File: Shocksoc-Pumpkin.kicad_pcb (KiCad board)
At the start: 2 copper layers, 98.7 x 98.5 mm, 45 parts, among them J1 USB_B_Micro, J2 Conn_01x03_Male, J3 Conn_01x02_Male, J4 Conn_ARM_JTAG_SWD_10, Q1 BSN20, SW1 SW_Push, SW2 SW_Push, SW3 SW_Push, SW4 SW_Push, U1 AP2202K-3.3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

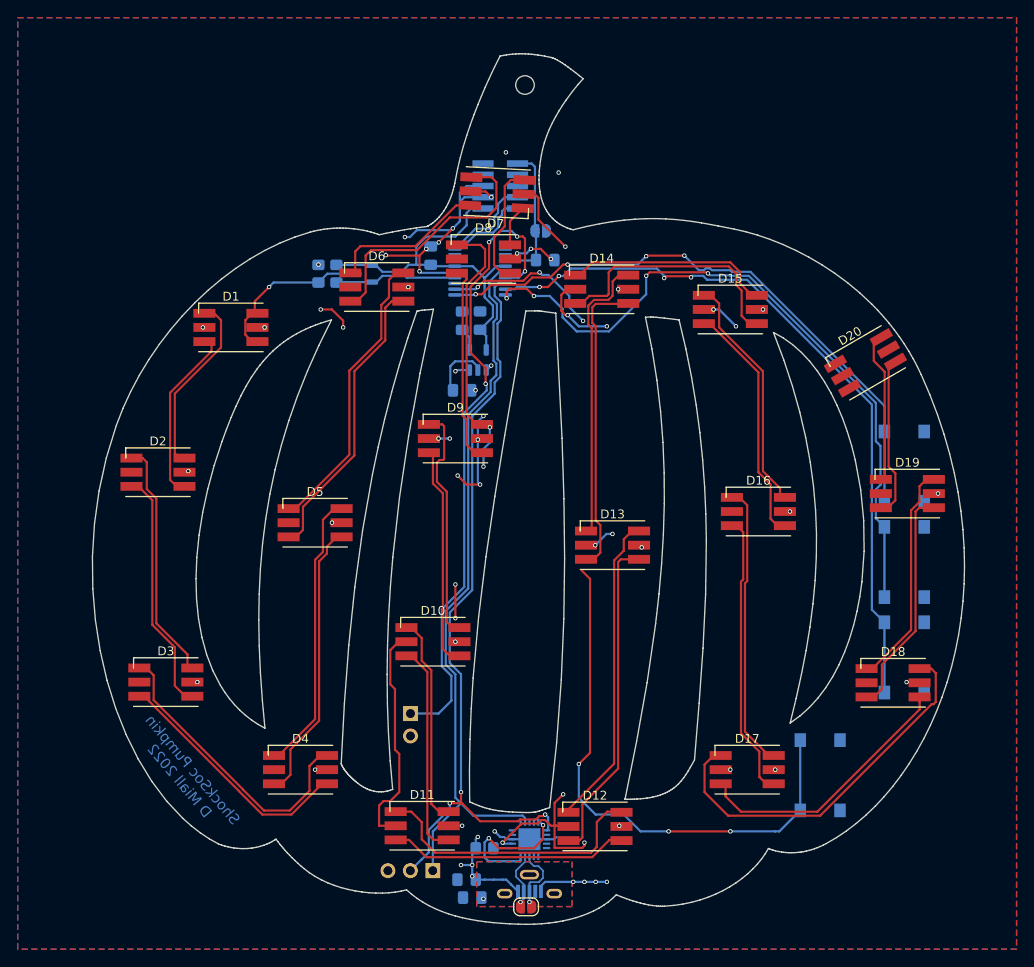
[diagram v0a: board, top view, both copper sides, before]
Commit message: Resized pads
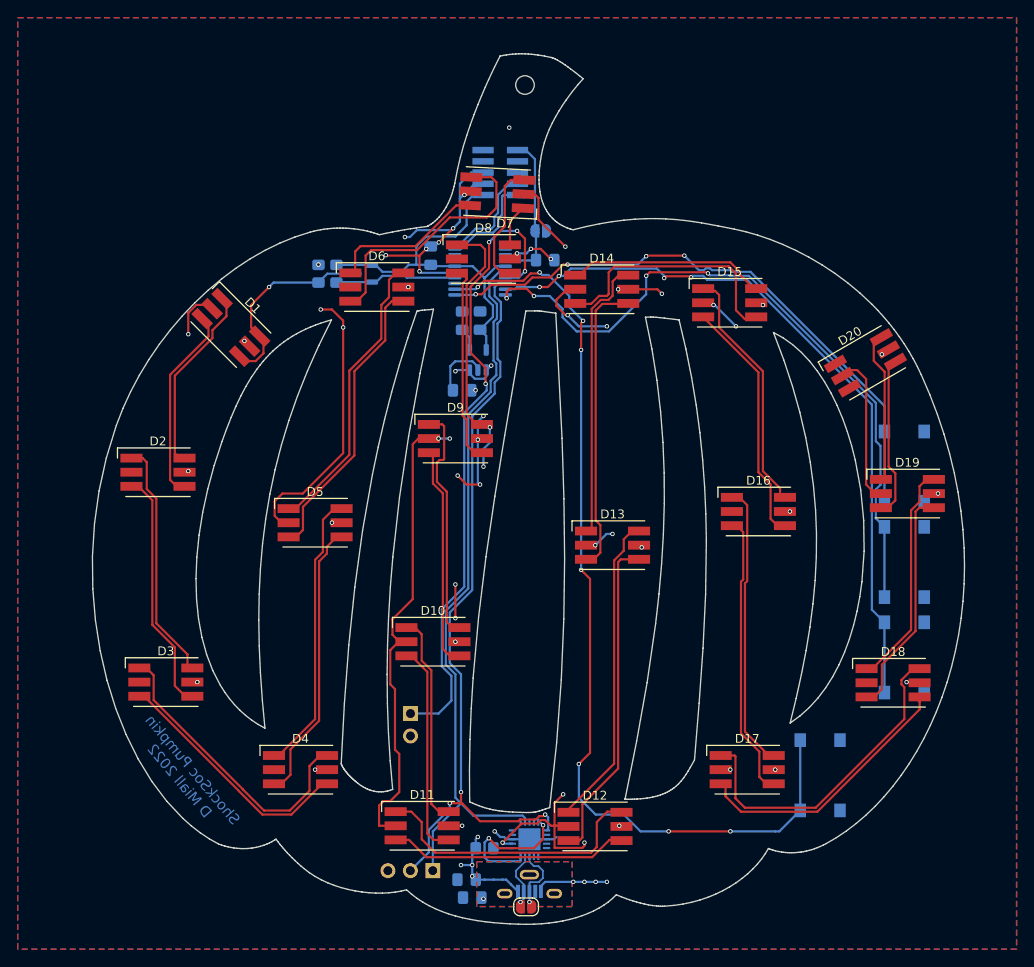
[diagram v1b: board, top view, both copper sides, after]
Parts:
- moved J4 1.52 mm to (92.7, 48.0)
- moved D15 0.77 mm to (118.7, 62.7)
- turned D1 to -45 degrees
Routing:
- net +5V: track 93.4 -> 174.5 mm, vias 25 -> 24
- net /3v3 MCU/btnD: track 80.6 -> 108.9 mm, vias 6 -> 8
- net Net-(D17-Pad1): track 43.3 -> 37.3 mm
- net /neopixel string/pxCtrl: track 18.4 -> 22.6 mm
- net GND: track 90.4 -> 93.7 mm, vias 38 -> 40
- net Net-(D1-Pad3): track 19.0 -> 21.7 mm
- net /3v3 MCU/swdio: track 9.83 -> 11.4 mm
- net Net-(D1-Pad1): track 19.4 -> 20.9 mm
- net Net-(D15-Pad1): track 26.4 -> 27.8 mm
- net +3.3V: track 42.6 -> 44.0 mm
- net /3v3 MCU/swclk: track 10.5 -> 11.7 mm
- net /3v3 MCU/rst: track 16.2 -> 17.4 mm
- net unconnected-(J4-Pad8): track 0.95 -> 0.00 mm
- net Net-(D15-Pad3): track 26.4 -> 27.3 mm
- net Net-(D13-Pad1): track 31.9 -> 31.1 mm
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
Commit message: Gerbers
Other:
- board text added: "ShockSoc Pumpkin V2 D Miall 2022"
- board text removed: "ShockSoc Pumpkin D Miall 2022"
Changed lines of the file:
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@@
   (gr_line (start 133.881078 90.85315) (end 133.833389 87.362595) (layer "Edge.Cuts") (width 0.15))
   (gr_line (start 102.498533 54.102398) (end 100.947157 54.48113) (layer "Edge.Cuts") (width 0.15))
-  (gr_text "ShockSoc Pumpkin\nD Miall 2022" (at 57.15 116.205 -50) (layer "B.Cu")
+  (gr_text "ShockSoc Pumpkin V2\nD Miall 2022" (at 57.15 116.205 -50) (layer "B.Cu")
     (effects (font (size 1.2 1.2) (thickness 0.3)) (justify mirror))
   )
@@
     (effects (font (size 1 1) (thickness 0.25)) (justify mirror))
   )
-  (gr_text "ShockSoc Pumpkin\nD Miall 2022" (at 57.15 116.205 -50) (layer "B.Mask")
+  (gr_text "ShockSoc Pumpkin V2\nD Miall 2022" (at 57.15 116.205 -50) (layer "B.Mask")
     (effects (font (size 1.2 1.2) (thickness 0.3)) (justify mirror))
   )

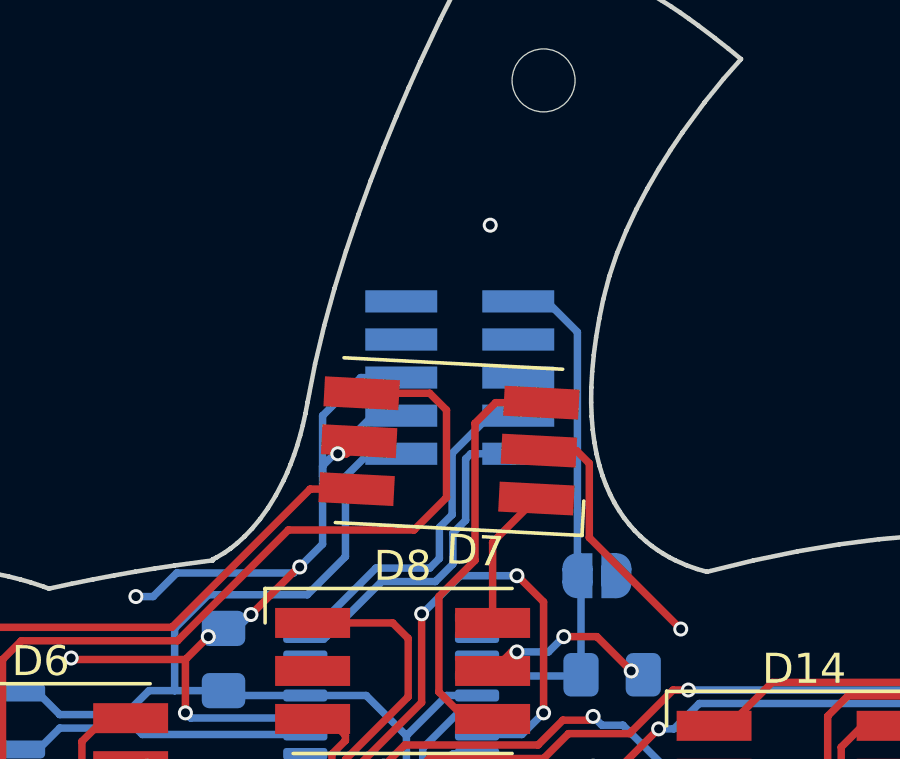
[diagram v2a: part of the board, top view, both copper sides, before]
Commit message: Add THT debug
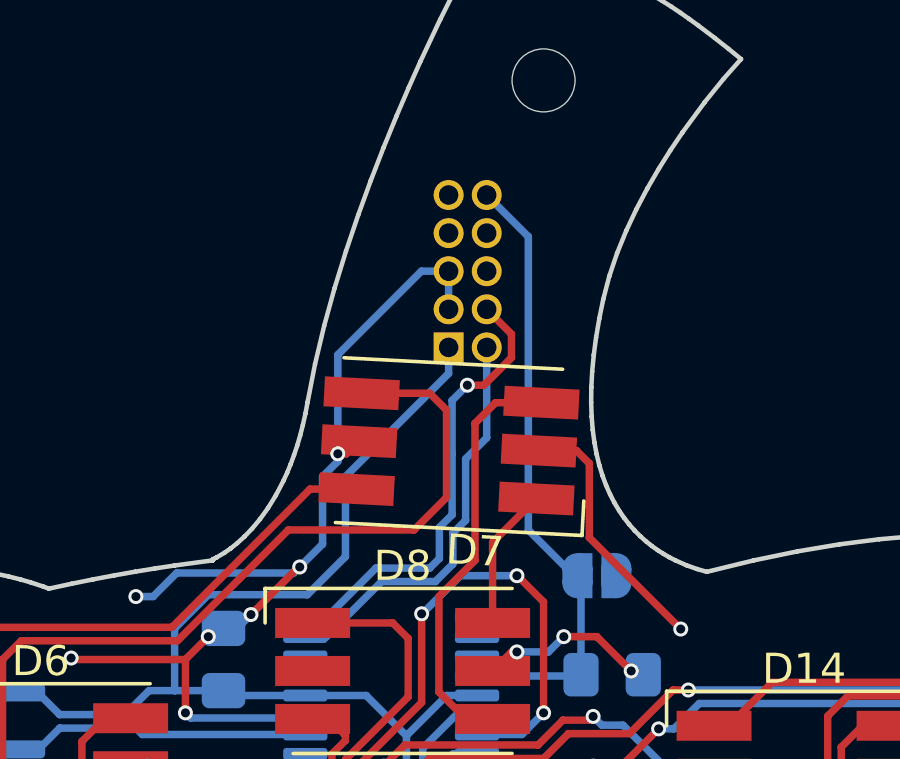
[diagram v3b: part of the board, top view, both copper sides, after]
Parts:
- J4: footprint Connector_PinHeader_1.27mm:PinHeader_2x05_P1.27mm_Vertical_SMD -> Connector_PinHeader_1.27mm:PinHeader_2x05_P1.27mm_Vertical
- moved J4 1.07 mm to (92.3, 47.0)
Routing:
- net /3v3 MCU/swclk: track 11.7 -> 15.2 mm, vias 0 -> 1
- net +3.3V: track 44.0 -> 47.5 mm
- net /3v3 MCU/rst: track 17.4 -> 20.8 mm
- net /3v3 MCU/swdio: track 11.4 -> 13.6 mm
- net GND: track 93.7 -> 95.2 mm, vias 40 -> 39
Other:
- board text added: "3v3"
- board text added: "GND"
- board text added: "RST"
- board text added: "SWCLK"
- board text added: "SWDIO"

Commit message: Prod
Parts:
- removed D11, D12, D13, D14, D15, D16, D17, D18, D19, D20: WS2813B, Library:LED_WS2813_hand
- removed MNT: MountingHole_2.1mm, MountingHole:MountingHole_2.1mm
- added REF**: MountingHole_2.2mm_M2, MountingHole:MountingHole_2.2mm_M2, F.Cu at (95.5, 38.1)
- moved D6 65.8 mm to (103.4, 121.9)
- moved D4 61.8 mm to (90.6, 57.3)
- moved D10 57.5 mm to (137.5, 77.5)
- moved D9 56.9 mm to (131.3, 114.6)
- moved D8 45.8 mm to (121.9, 91.4)
- moved D7 29.0 mm to (118.4, 63.0), turned to 0 degrees
- moved D3 16.5 mm to (66.6, 117.3)
- moved D5 14.4 mm to (85.7, 91.4)
- moved D2 9.38 mm to (52.6, 91.2)
- moved D1 2.05 mm to (61.2, 67.3), turned to 0 degrees
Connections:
- D10 pad 1: Net-(D10-Pad1) -> unconnected-(D10-Pad1)
- D10 pad 3: Net-(D10-Pad3) -> unconnected-(D10-Pad3)
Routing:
- net Net-(D6-Pad1): track 17.6 -> 78.4 mm
- net Net-(D3-Pad3): track 27.1 -> 85.9 mm
- net Net-(D6-Pad3): track 29.3 -> 83.9 mm
- net +5V: track 174.5 -> 120.2 mm, vias 24 -> 21
- net Net-(D3-Pad1): track 32.7 -> 79.9 mm
- net Net-(D17-Pad1): track 37.3 -> 0.00 mm
- net Net-(D12-Pad3): track 36.5 -> 0.00 mm
- net Net-(D5-Pad1): track 31.9 -> 67.9 mm
- net Net-(D12-Pad1): track 35.1 -> 0.00 mm
- net Net-(D13-Pad3): track 32.3 -> 0.00 mm
- net Net-(D11-Pad1): track 32.2 -> 0.00 mm
- net Net-(D13-Pad1): track 31.1 -> 0.00 mm
- net Net-(D16-Pad3): track 31.1 -> 0.00 mm
- net Net-(D16-Pad1): track 31.1 -> 0.00 mm
- net Net-(D17-Pad3): track 30.5 -> 0.00 mm
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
